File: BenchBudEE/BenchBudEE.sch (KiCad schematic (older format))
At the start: 0 parts

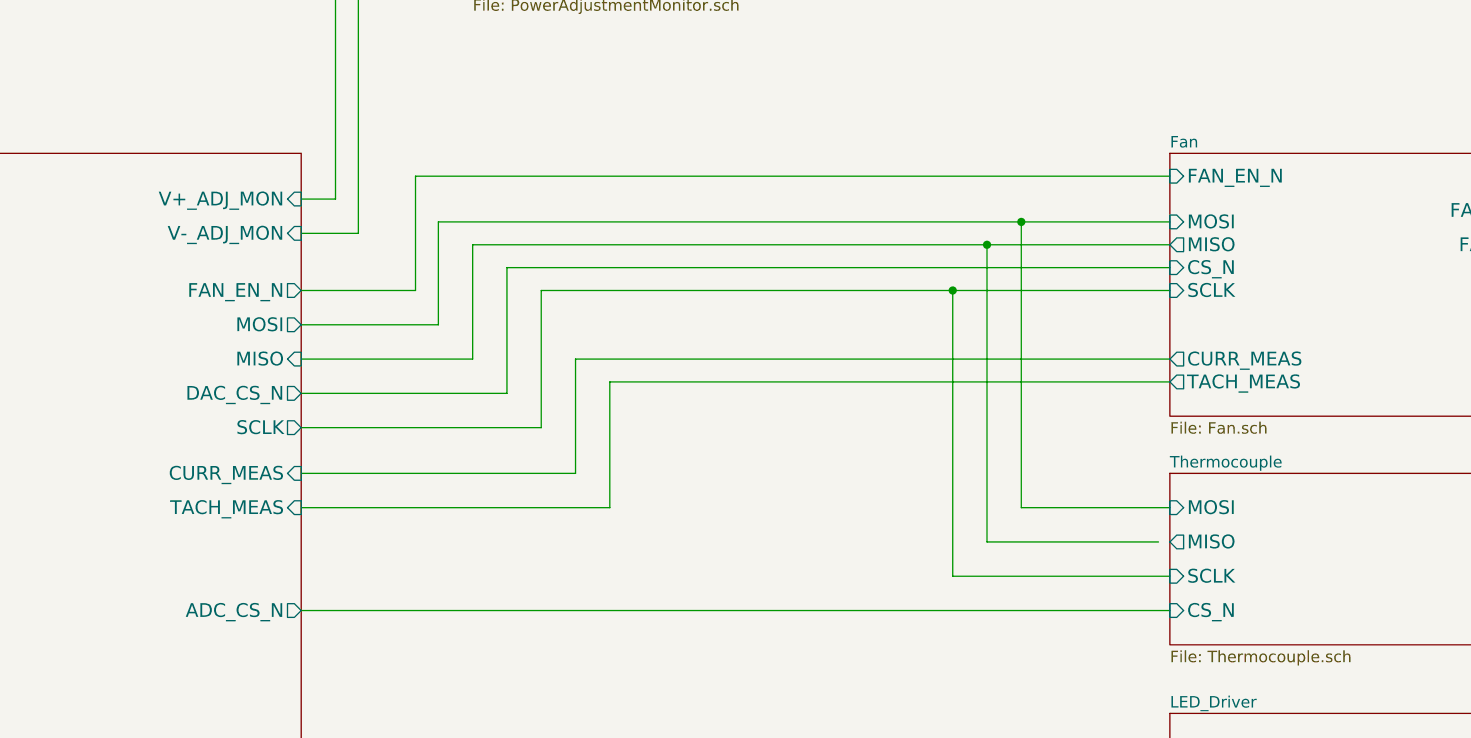
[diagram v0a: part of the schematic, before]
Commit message: Fan/current module refactoring
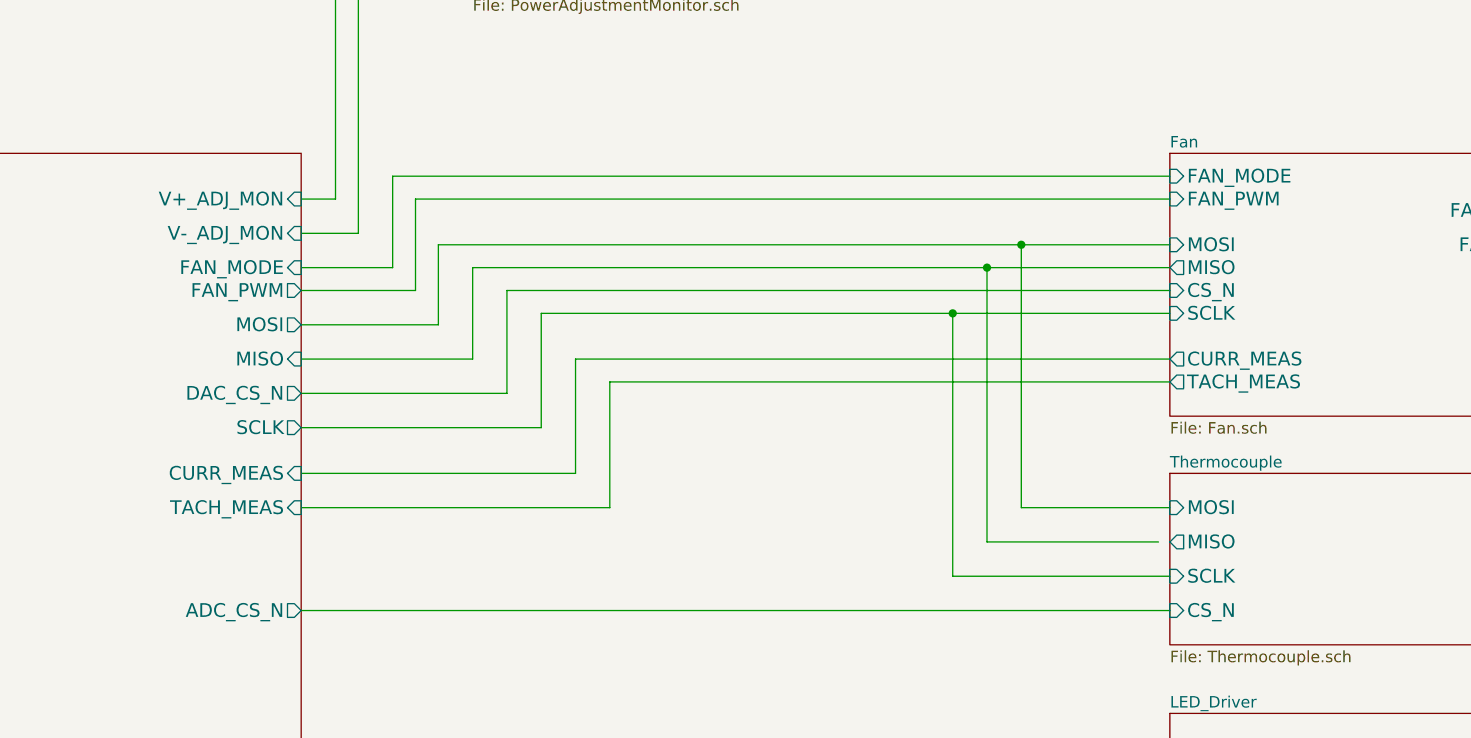
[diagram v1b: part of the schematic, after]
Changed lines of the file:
@@
 Sheet 1 9
 Title ""
-Date "9 feb 2014"
+Date "11 feb 2014"
 Rev ""
 Comp ""
@@
 F5 "RELAY+" I L 7100 6150 60
 F6 "RELAY-" O L 7100 6300 60
-$EndSheet
-$Sheet
-S 7100 2750 1750 1150
-U 52ED1CA7
-F0 "Fan" 50
-F1 "Fan.sch" 50
-F2 "MOSI" I L 7100 3050 60
-F3 "MISO" O L 7100 3150 60
-F4 "CS_N" I L 7100 3250 60
-F5 "SCLK" I L 7100 3350 60
-F6 "FAN_OUT+" O R 8850 3000 60
-F7 "TACH_IN" I R 8850 3600 60
-F8 "TACH_MEAS" O L 7100 3750 60
-F9 "FAN_EN_N" I L 7100 2850 60
-F10 "CURR_MEAS" O L 7100 3650 60
-F11 "FAN_OUT-" O R 8850 3150 60
 $EndSheet
 $Sheet
@@
 F6 "RELAY+" O R 3300 6150 60
 F7 "RELAY-" O R 3300 6300 60
-F8 "FAN_EN_N" O R 3300 3350 60
-F9 "CURR_MEAS" I R 3300 4150 60
-F10 "V+_ADJ_MON" I R 3300 2950 60
-F11 "V-_ADJ_MON" I R 3300 3100 60
-F12 "LED_EN_PWM" O R 3300 5350 60
-F13 "DAC_CS_N" O R 3300 3800 60
-F14 "ADC_CS_N" O R 3300 4750 60
+F8 "CURR_MEAS" I R 3300 4150 60
+F9 "V+_ADJ_MON" I R 3300 2950 60
+F10 "V-_ADJ_MON" I R 3300 3100 60
+F11 "LED_EN_PWM" O R 3300 5350 60
+F12 "DAC_CS_N" O R 3300 3800 60
+F13 "ADC_CS_N" O R 3300 4750 60
+F14 "FAN_PWM" O R 3300 3350 60
+F15 "FAN_MODE" I R 3300 3250 60
 $EndSheet
 Wire Wire Line
@@
 	3300 3350 3800 3350
 Wire Wire Line
-	3800 3350 3800 2850
-Wire Wire Line
-	3800 2850 7100 2850
+	3800 3350 3800 2950
+Wire Wire Line
+	3800 2950 7100 2950
 Wire Wire Line
 	3300 3500 3900 3500
 Wire Wire Line
-	3900 3500 3900 3050
-Wire Wire Line
-	3900 3050 7100 3050
-Wire Wire Line
-	4050 3150 7100 3150
-Wire Wire Line
-	4050 3150 4050 3650
+	3900 3500 3900 3150
+Wire Wire Line
+	3900 3150 7100 3150
+Wire Wire Line
+	4050 3250 7100 3250
 Wire Wire Line
 	4050 3650 3300 3650
@@
 	3300 3800 4200 3800
 Wire Wire Line
-	4200 3800 4200 3250
-Wire Wire Line
-	4200 3250 7100 3250
+	4200 3800 4200 3350
+Wire Wire Line
+	4200 3350 7100 3350
 Wire Wire Line
 	3300 3950 4350 3950
 Wire Wire Line
-	4350 3950 4350 3350
-Wire Wire Line
-	4350 3350 7100 3350
+	4350 3450 7100 3450
 Wire Wire Line
 	3300 4150 4500 4150
@@
 	7100 4300 6450 4300
 Wire Wire Line
-	6450 4300 6450 3050
-Connection ~ 6450 3050
+	6450 4300 6450 3150
+Connection ~ 6450 3150
 Wire Wire Line
 	7050 4450 6300 4450
 Wire Wire Line
-	6300 4450 6300 3150
-Connection ~ 6300 3150
+	6300 4450 6300 3250
+Connection ~ 6300 3250
 Wire Wire Line
 	7100 4600 6150 4600
 Wire Wire Line
-	6150 4600 6150 3350
-Connection ~ 6150 3350
+	6150 4600 6150 3450
+Connection ~ 6150 3450
 Wire Wire Line
 	3300 4750 7100 4750
@@
 Wire Wire Line
 	3300 5350 7100 5350
+$Sheet
+S 7100 2750 1750 1150
+U 52ED1CA7
+F0 "Fan" 50
+F1 "Fan.sch" 50
+F2 "MOSI" I L 7100 3150 60
+F3 "MISO" O L 7100 3250 60
+F4 "CS_N" I L 7100 3350 60
+F5 "SCLK" I L 7100 3450 60
+F6 "FAN_OUT+" O R 8850 3000 60
+F7 "TACH_IN" I R 8850 3600 60
+F8 "TACH_MEAS" O L 7100 3750 60
+F9 "CURR_MEAS" O L 7100 3650 60
+F10 "FAN_OUT-" O R 8850 3150 60
+F11 "FAN_PWM" I L 7100 2950 60
+F12 "FAN_MODE" I L 7100 2850 60
+$EndSheet
+Wire Wire Line
+	4050 3250 4050 3650
+Wire Wire Line
+	4350 3950 4350 3450
+Wire Wire Line
+	3700 2850 7100 2850
+Wire Wire Line
+	3700 2850 3700 3250
+Wire Wire Line
+	3700 3250 3300 3250
 $EndSCHEMATC

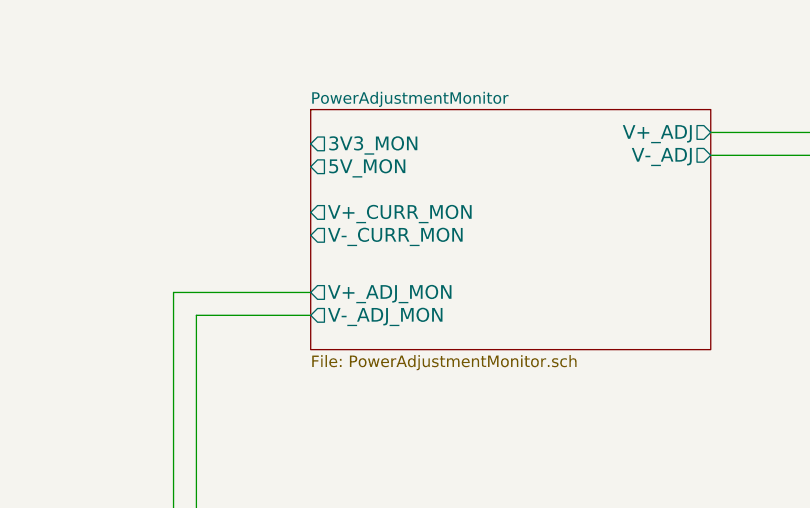
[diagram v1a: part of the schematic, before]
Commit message: PCB Outline created and changes during  components choice
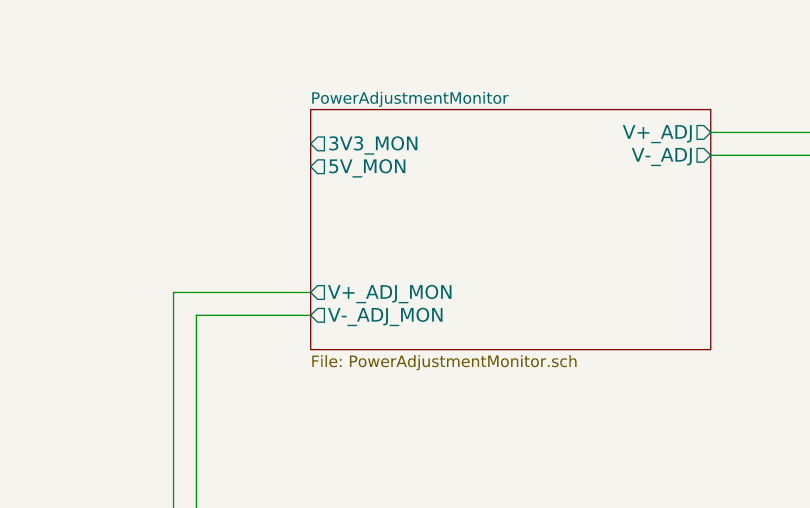
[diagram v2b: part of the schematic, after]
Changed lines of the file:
@@
 Sheet 1 9
 Title ""
-Date "11 feb 2014"
+Date "16 feb 2014"
 Rev ""
 Comp ""
@@
 F6 "V+_ADJ_MON" O L 4050 1800 60
 F7 "V-_ADJ_MON" O L 4050 1900 60
-F8 "V+_CURR_MON" O L 4050 1450 60
-F9 "V-_CURR_MON" O L 4050 1550 60
 $EndSheet
 Wire Wire Line

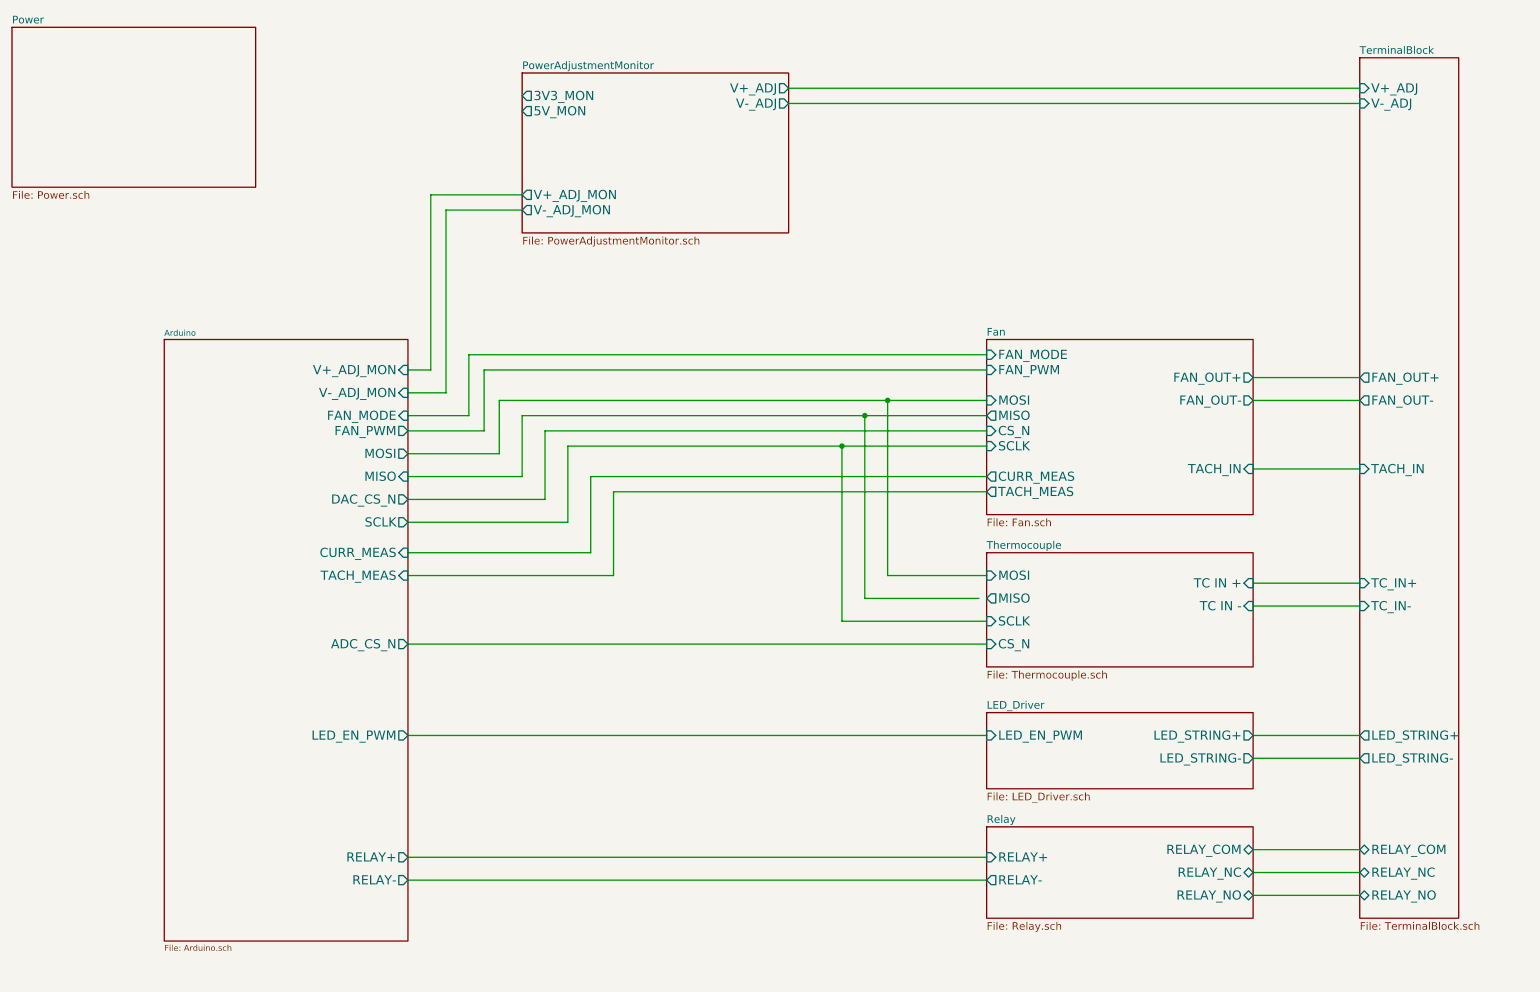
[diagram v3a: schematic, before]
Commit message: Associating and Placingthe Thermocouple Module
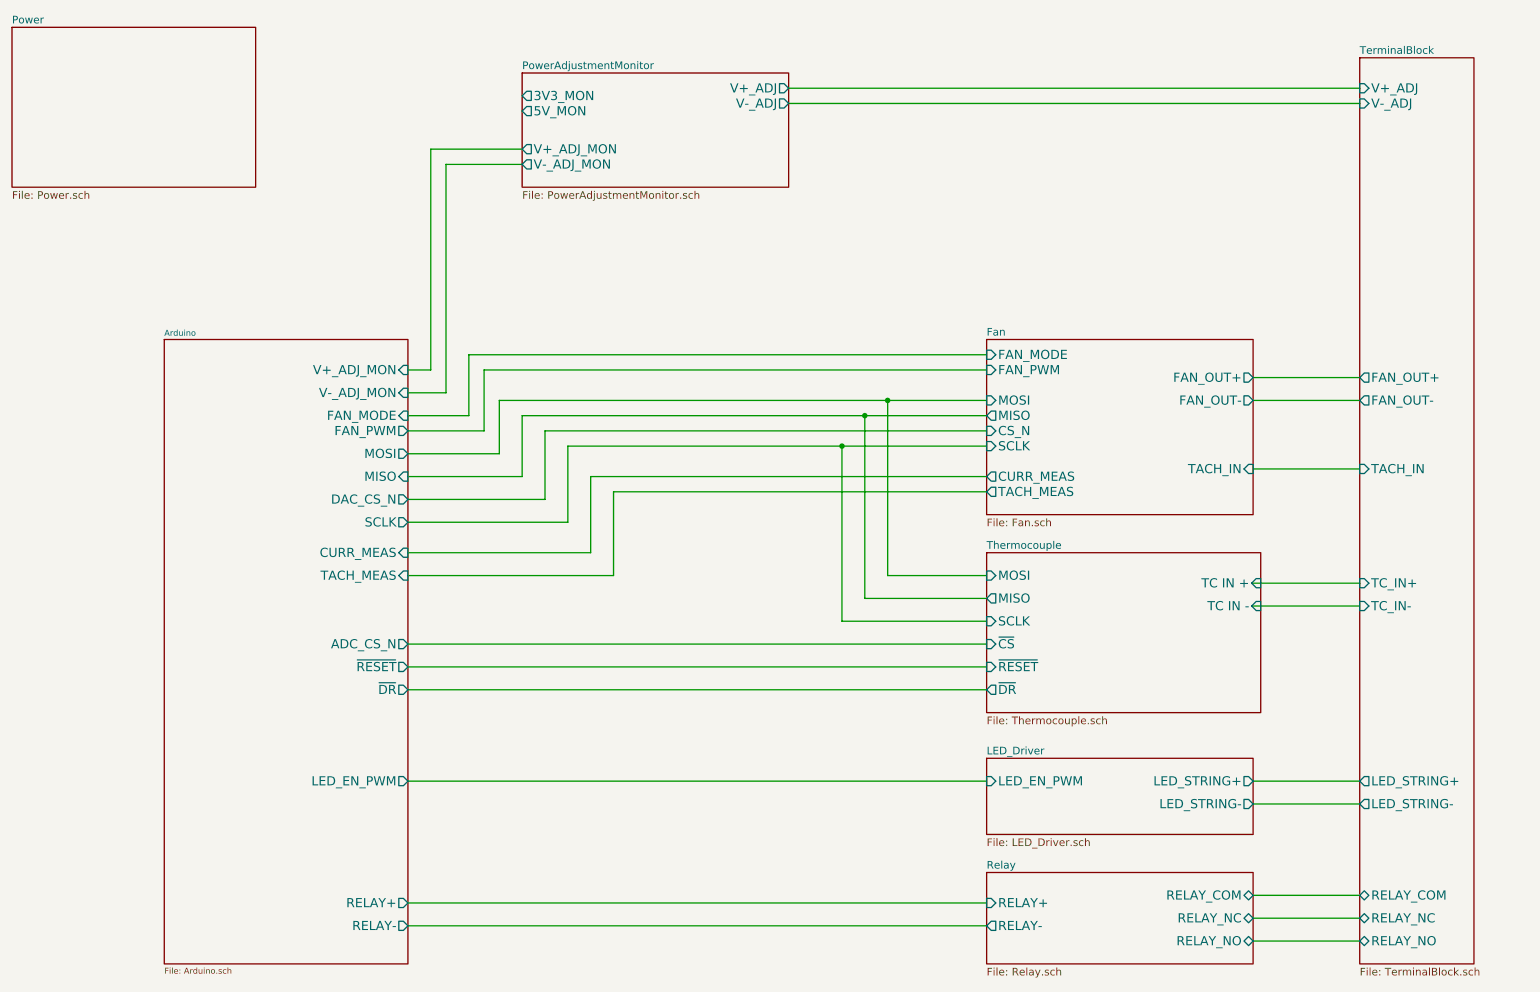
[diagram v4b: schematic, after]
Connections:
- wire segments 52 -> 54
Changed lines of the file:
@@
 Sheet 1 9
 Title ""
-Date "17 feb 2014"
+Date "19 feb 2014"
 Rev ""
 Comp ""
@@
 $EndDescr
 $Sheet
-S 7100 4150 1750 750
+S 7100 4150 1800 1050
 U 52ED1C3D
 F0 "Thermocouple" 50
 F1 "Thermocouple.sch" 50
-F2 "TC IN +" I R 8850 4350 60
-F3 "TC IN -" I R 8850 4500 60
+F2 "TC IN +" I R 8900 4350 60
+F3 "TC IN -" I R 8900 4500 60
 F4 "MOSI" I L 7100 4300 60
 F5 "MISO" O L 7100 4450 60
 F6 "SCLK" I L 7100 4600 60
-F7 "CS_N" I L 7100 4750 60
-$EndSheet
-$Sheet
-S 7100 5200 1750 500
+F7 "~CS" I L 7100 4750 60
+F8 "~RESET" I L 7100 4900 60
+F9 "~DR" O L 7100 5050 60
+$EndSheet
+$Sheet
+S 7100 5500 1750 500
 U 52ED1C90
 F0 "LED_Driver" 50
 F1 "LED_Driver.sch" 50
-F2 "LED_EN_PWM" I L 7100 5350 60
-F3 "LED_STRING+" O R 8850 5350 60
-F4 "LED_STRING-" O R 8850 5500 60
+F2 "LED_EN_PWM" I L 7100 5650 60
+F3 "LED_STRING+" O R 8850 5650 60
+F4 "LED_STRING-" O R 8850 5800 60
 $EndSheet
 $Sheet
@@
 $EndSheet
 $Sheet
-S 7100 5950 1750 600
+S 7100 6250 1750 600
 U 52ED1C4D
 F0 "Relay" 50
 F1 "Relay.sch" 50
-F2 "RELAY_NC" B R 8850 6250 60
-F3 "RELAY_NO" B R 8850 6400 60
-F4 "RELAY_COM" B R 8850 6100 60
-F5 "RELAY+" I L 7100 6150 60
-F6 "RELAY-" O L 7100 6300 60
-$EndSheet
-$Sheet
-S 9550 900  650  5650
+F2 "RELAY_NC" B R 8850 6550 60
+F3 "RELAY_NO" B R 8850 6700 60
+F4 "RELAY_COM" B R 8850 6400 60
+F5 "RELAY+" I L 7100 6450 60
+F6 "RELAY-" O L 7100 6600 60
+$EndSheet
+$Sheet
+S 9550 900  750  5950
 U 52ED1CD3
 F0 "TerminalBlock" 50
@@
 F3 "V-_ADJ" I L 9550 1200 60
 F4 "TACH_IN" I L 9550 3600 60
-F5 "LED_STRING+" O L 9550 5350 60
-F6 "LED_STRING-" O L 9550 5500 60
+F5 "LED_STRING+" O L 9550 5650 60
+F6 "LED_STRING-" O L 9550 5800 60
 F7 "TC_IN+" I L 9550 4350 60
 F8 "TC_IN-" I L 9550 4500 60
-F9 "RELAY_COM" B L 9550 6100 60
-F10 "RELAY_NC" B L 9550 6250 60
-F11 "RELAY_NO" B L 9550 6400 60
+F9 "RELAY_COM" B L 9550 6400 60
+F10 "RELAY_NC" B L 9550 6550 60
+F11 "RELAY_NO" B L 9550 6700 60
 F12 "FAN_OUT+" O L 9550 3000 60
 F13 "FAN_OUT-" O L 9550 3150 60
@@
 	8850 3600 9550 3600
 Wire Wire Line
-	8850 6100 9550 6100
-Wire Wire Line
-	9550 6250 8850 6250
-Wire Wire Line
 	8850 6400 9550 6400
-$Sheet
-S 1700 2750 1600 3950
+Wire Wire Line
+	9550 6550 8850 6550
+Wire Wire Line
+	8850 6700 9550 6700
+$Sheet
+S 1700 2750 1600 4100
 U 52ED1BFA
 F0 "Arduino" 39
@@
 F4 "SCLK" O R 3300 3950 60
 F5 "TACH_MEAS" I R 3300 4300 60
-F6 "RELAY+" O R 3300 6150 60
-F7 "RELAY-" O R 3300 6300 60
+F6 "RELAY+" O R 3300 6450 60
+F7 "RELAY-" O R 3300 6600 60
 F8 "CURR_MEAS" I R 3300 4150 60
 F9 "V+_ADJ_MON" I R 3300 2950 60
 F10 "V-_ADJ_MON" I R 3300 3100 60
-F11 "LED_EN_PWM" O R 3300 5350 60
+F11 "LED_EN_PWM" O R 3300 5650 60
 F12 "DAC_CS_N" O R 3300 3800 60
 F13 "ADC_CS_N" O R 3300 4750 60
 F14 "FAN_PWM" O R 3300 3350 60
 F15 "FAN_MODE" I R 3300 3250 60
+F16 "~DR" O R 3300 5050 60
+F17 "~RESET" O R 3300 4900 60
 $EndSheet
 Wire Wire Line
@@
 	9550 4500 8850 4500
 Wire Wire Line
-	9550 5350 8850 5350
-Wire Wire Line
-	8850 5500 9550 5500
-$Sheet
-S 4050 1000 1750 1050
+	9550 5650 8850 5650
+Wire Wire Line
+	8850 5800 9550 5800
+$Sheet
+S 4050 1000 1750 750
 U 52F64583
 F0 "PowerAdjustmentMonitor" 50
@@
 F4 "3V3_MON" O L 4050 1150 60
 F5 "5V_MON" O L 4050 1250 60
-F6 "V+_ADJ_MON" O L 4050 1800 60
-F7 "V-_ADJ_MON" O L 4050 1900 60
+F6 "V+_ADJ_MON" O L 4050 1500 60
+F7 "V-_ADJ_MON" O L 4050 1600 60
 $EndSheet
 Wire Wire Line
 	3300 2950 3450 2950
 Wire Wire Line
-	3450 2950 3450 1800
-Wire Wire Line
-	3450 1800 4050 1800
-Wire Wire Line
-	3550 1900 4050 1900
-Wire Wire Line
-	3550 1900 3550 3100
+	3450 2950 3450 1500
+Wire Wire Line
+	3450 1500 4050 1500
+Wire Wire Line
+	3550 1600 4050 1600
+Wire Wire Line
+	3550 1600 3550 3100
 Wire Wire Line
 	3550 3100 3300 3100
@@
 Connection ~ 6450 3150
 Wire Wire Line
-	7050 4450 6300 4450
+	6300 4450 7100 4450
 Wire Wire Line
 	6300 4450 6300 3250
@@
 	3300 4750 7100 4750
 Wire Wire Line
-	7100 6300 3300 6300
-Wire Wire Line
-	3300 6150 7100 6150
-Wire Wire Line
-	3300 5350 7100 5350
+	7100 6600 3300 6600
+Wire Wire Line
+	3300 6450 7100 6450
+Wire Wire Line
+	3300 5650 7100 5650
 $Sheet
 S 7100 2750 1750 1150
@@
 Wire Wire Line
 	3700 3250 3300 3250
+Wire Wire Line
+	3300 4900 7100 4900
+Wire Wire Line
+	3300 5050 7100 5050
 $EndSCHEMATC
